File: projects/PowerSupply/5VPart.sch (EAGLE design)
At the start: 26 parts, among them IC1 LM2596T, IC2 LM2596T, X1 PWR-IN, X3 PWR-OUT

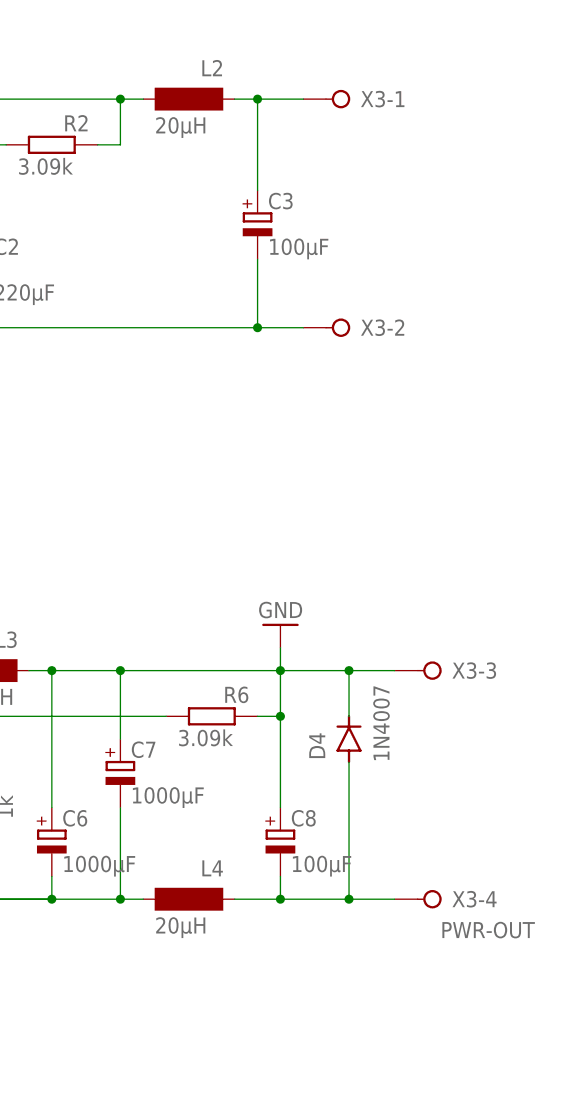
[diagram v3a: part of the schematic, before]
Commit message: feat: 5 volt part modified
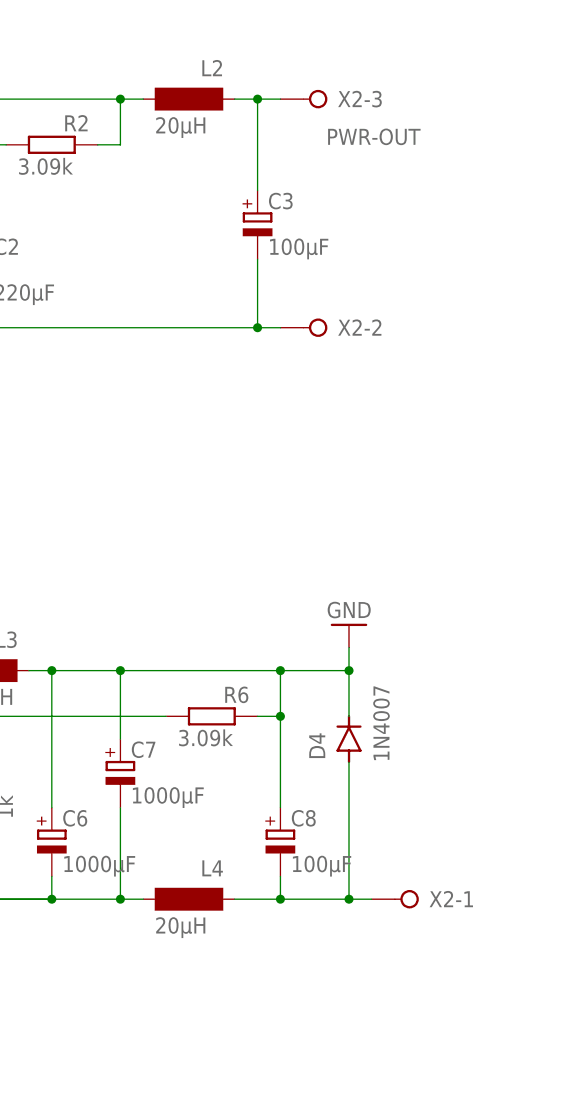
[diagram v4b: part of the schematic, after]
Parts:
- removed X3: PWR-OUT, con-wago-508:W237-04P
- added X2: PWR-OUT, con-wago-508:W237-03P
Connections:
- net GND: now also X2-2.KL; no longer X3-2.KL, X3-3.KL
- net N$3: now also X2-1.KL; no longer X3-4.KL
- net N$7: now also X2-3.KL; no longer X3-1.KL
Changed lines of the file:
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@@
 <part name="C2" library="rcl" library_urn="urn:adsk.eagle:library:334" deviceset="CPOL-EU" device="E2.5-6" package3d_urn="urn:adsk.eagle:package:23349/1" value="220µF"/>
 <part name="L1" library="bb84" deviceset="IND-120-330K" device="" value="33µH"/>
-<part name="X3" library="con-wago-508" library_urn="urn:adsk.eagle:library:196" deviceset="W237-04P" device="" package3d_urn="urn:adsk.eagle:package:10735/1" value="PWR-OUT"/>
 <part name="C3" library="rcl" library_urn="urn:adsk.eagle:library:334" deviceset="CPOL-EU" device="E2.5-6" package3d_urn="urn:adsk.eagle:package:23349/1" value="100µF"/>
 <part name="L2" library="bb84" deviceset="B82111B0000C020" device="" value="20µH"/>
@@
 <part name="GND2" library="supply1" library_urn="urn:adsk.eagle:library:371" deviceset="GND" device=""/>
 <part name="GND3" library="supply1" library_urn="urn:adsk.eagle:library:371" deviceset="GND" device=""/>
-<part name="GND4" library="supply1" library_urn="urn:adsk.eagle:library:371" deviceset="GND" device=""/>
 <part name="P+1" library="supply1" library_urn="urn:adsk.eagle:library:371" deviceset="VCC" device=""/>
 <part name="P+2" library="supply1" library_urn="urn:adsk.eagle:library:371" deviceset="VCC" device=""/>
@@
 <part name="D2" library="Diodes" library_urn="urn:adsk.eagle:library:11396254" deviceset="1N4007" device="" package3d_urn="urn:adsk.eagle:package:10898391/4"/>
 <part name="D4" library="Diodes" library_urn="urn:adsk.eagle:library:11396254" deviceset="1N4007" device="" package3d_urn="urn:adsk.eagle:package:10898391/4"/>
+<part name="X2" library="con-wago-508" library_urn="urn:adsk.eagle:library:196" deviceset="W237-03P" device="" package3d_urn="urn:adsk.eagle:package:10737/1" value="PWR-OUT"/>
+<part name="GND5" library="supply1" library_urn="urn:adsk.eagle:library:371" deviceset="GND" device=""/>
 </parts>
 <sheets>
@@
 <attribute name="NAME" x="125.73" y="157.48" size="1.778" layer="95"/>
 </instance>
-<instance part="X3" gate="-1" x="172.72" y="154.94" smashed="yes" rot="MR0">
-<attribute name="NAME" x="173.99" y="155.829" size="1.778" layer="95" rot="MR180"/>
-</instance>
-<instance part="X3" gate="-2" x="172.72" y="129.54" smashed="yes" rot="MR0">
-<attribute name="NAME" x="173.99" y="130.429" size="1.778" layer="95" rot="MR180"/>
-</instance>
-<instance part="X3" gate="-3" x="182.88" y="91.44" smashed="yes" rot="MR0">
-<attribute name="NAME" x="184.15" y="92.329" size="1.778" layer="95" rot="MR180"/>
-</instance>
-<instance part="X3" gate="-4" x="182.88" y="66.04" smashed="yes" rot="MR0">
-<attribute name="VALUE" x="182.88" y="63.5" size="1.778" layer="96" rot="MR180"/>
-<attribute name="NAME" x="184.15" y="66.929" size="1.778" layer="95" rot="MR180"/>
-</instance>
 <instance part="C3" gate="G$1" x="162.56" y="142.24" smashed="yes">
 <attribute name="NAME" x="163.703" y="142.7226" size="1.778" layer="95"/>
@@
 <attribute name="VALUE" x="73.66" y="121.92" size="1.778" layer="96"/>
 </instance>
-<instance part="GND4" gate="1" x="165.1" y="96.52" smashed="yes" rot="R180">
-<attribute name="VALUE" x="167.64" y="99.06" size="1.778" layer="96" rot="R180"/>
-</instance>
 <instance part="P+1" gate="VCC" x="30.48" y="35.56" smashed="yes" rot="R270">
 <attribute name="VALUE" x="27.94" y="38.1" size="1.778" layer="96"/>
@@
 <attribute name="NAME" x="170.0784" y="81.5086" size="1.778" layer="95" rot="R90"/>
 <attribute name="VALUE" x="177.2158" y="81.2546" size="1.778" layer="96" rot="R90"/>
+</instance>
+<instance part="X2" gate="-1" x="180.34" y="66.04" smashed="yes" rot="MR0">
+<attribute name="NAME" x="181.61" y="66.929" size="1.778" layer="95" rot="MR180"/>
+</instance>
+<instance part="X2" gate="-2" x="170.18" y="129.54" smashed="yes" rot="MR0">
+<attribute name="NAME" x="171.45" y="130.429" size="1.778" layer="95" rot="MR180"/>
+</instance>
+<instance part="X2" gate="-3" x="170.18" y="154.94" smashed="yes" rot="MR0">
+<attribute name="VALUE" x="170.18" y="149.86" size="1.778" layer="96"/>
+<attribute name="NAME" x="171.45" y="155.829" size="1.778" layer="95" rot="MR180"/>
+</instance>
+<instance part="GND5" gate="1" x="172.72" y="96.52" smashed="yes" rot="R180">
+<attribute name="VALUE" x="175.26" y="99.06" size="1.778" layer="96" rot="R180"/>
 </instance>
 </instances>
@@
 </segment>
 <segment>
-<pinref part="X3" gate="-2" pin="KL"/>
-<wire x1="167.64" y1="129.54" x2="162.56" y2="129.54" width="0.1524" layer="91"/>
 <pinref part="C3" gate="G$1" pin="-"/>
 <wire x1="162.56" y1="137.16" x2="162.56" y2="129.54" width="0.1524" layer="91"/>
-<junction x="162.56" y="129.54"/>
 <pinref part="IC1" gate="G$1" pin="GND"/>
 <wire x1="88.9" y1="147.32" x2="86.36" y2="147.32" width="0.1524" layer="91"/>
@@
 <wire x1="86.36" y1="152.4" x2="86.36" y2="147.32" width="0.1524" layer="91"/>
 <junction x="86.36" y="147.32"/>
+<pinref part="X2" gate="-2" pin="KL"/>
+<wire x1="165.1" y1="129.54" x2="162.56" y2="129.54" width="0.1524" layer="91"/>
+<junction x="162.56" y="129.54"/>
 </segment>
 <segment>
@@
 <segment>
 <pinref part="C6" gate="G$1" pin="+"/>
-<pinref part="X3" gate="-3" pin="KL"/>
 <wire x1="147.32" y1="91.44" x2="165.1" y2="91.44" width="0.1524" layer="91"/>
 <pinref part="C7" gate="G$1" pin="+"/>
 <wire x1="165.1" y1="91.44" x2="172.72" y2="91.44" width="0.1524" layer="91"/>
-<wire x1="172.72" y1="91.44" x2="177.8" y2="91.44" width="0.1524" layer="91"/>
 <wire x1="147.32" y1="83.82" x2="147.32" y2="91.44" width="0.1524" layer="91"/>
 <junction x="147.32" y="91.44"/>
@@
 <junction x="139.7" y="91.44"/>
 <wire x1="139.7" y1="91.44" x2="139.7" y2="76.2" width="0.1524" layer="91"/>
-<pinref part="GND4" gate="1" pin="GND"/>
-<wire x1="165.1" y1="93.98" x2="165.1" y2="91.44" width="0.1524" layer="91"/>
 <junction x="165.1" y="91.44"/>
 <pinref part="R6" gate="G$1" pin="2"/>
@@
 <pinref part="D4" gate="G$1" pin="C"/>
 <wire x1="172.72" y1="86.36" x2="172.72" y2="91.44" width="0.1524" layer="91"/>
+<pinref part="GND5" gate="1" pin="GND"/>
+<wire x1="172.72" y1="91.44" x2="172.72" y2="93.98" width="0.1524" layer="91"/>
 <junction x="172.72" y="91.44"/>
 </segment>
@@
 <net name="N$7" class="0">
 <segment>
-<pinref part="X3" gate="-1" pin="KL"/>
-<wire x1="167.64" y1="154.94" x2="162.56" y2="154.94" width="0.1524" layer="91"/>
 <pinref part="C3" gate="G$1" pin="+"/>
 <wire x1="162.56" y1="144.78" x2="162.56" y2="154.94" width="0.1524" layer="91"/>
 <pinref part="L2" gate="G$1" pin="2"/>
 <wire x1="160.02" y1="154.94" x2="162.56" y2="154.94" width="0.1524" layer="91"/>
+<pinref part="X2" gate="-3" pin="KL"/>
+<wire x1="165.1" y1="154.94" x2="162.56" y2="154.94" width="0.1524" layer="91"/>
 <junction x="162.56" y="154.94"/>
 </segment>
@@
 <segment>
 <pinref part="C8" gate="G$1" pin="-"/>
-<pinref part="X3" gate="-4" pin="KL"/>
 <wire x1="165.1" y1="66.04" x2="172.72" y2="66.04" width="0.1524" layer="91"/>
-<wire x1="172.72" y1="66.04" x2="177.8" y2="66.04" width="0.1524" layer="91"/>
 <wire x1="165.1" y1="66.04" x2="165.1" y2="68.58" width="0.1524" layer="91"/>
 <pinref part="L4" gate="G$1" pin="2"/>
@@
 <pinref part="D4" gate="G$1" pin="A"/>
 <wire x1="172.72" y1="81.28" x2="172.72" y2="66.04" width="0.1524" layer="91"/>
+<pinref part="X2" gate="-1" pin="KL"/>
+<wire x1="175.26" y1="66.04" x2="172.72" y2="66.04" width="0.1524" layer="91"/>
 <junction x="172.72" y="66.04"/>
 </segment>
